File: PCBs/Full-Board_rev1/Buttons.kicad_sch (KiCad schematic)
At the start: 4 parts, among them SW1 SW_MEC_5E, SW2 SW_MEC_5E

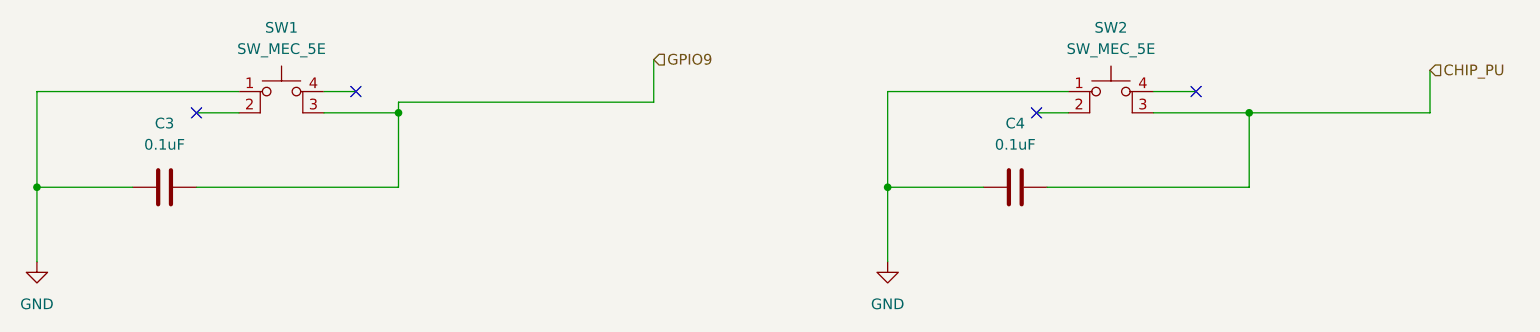
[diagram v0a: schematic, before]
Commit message: Added footprints for main board components
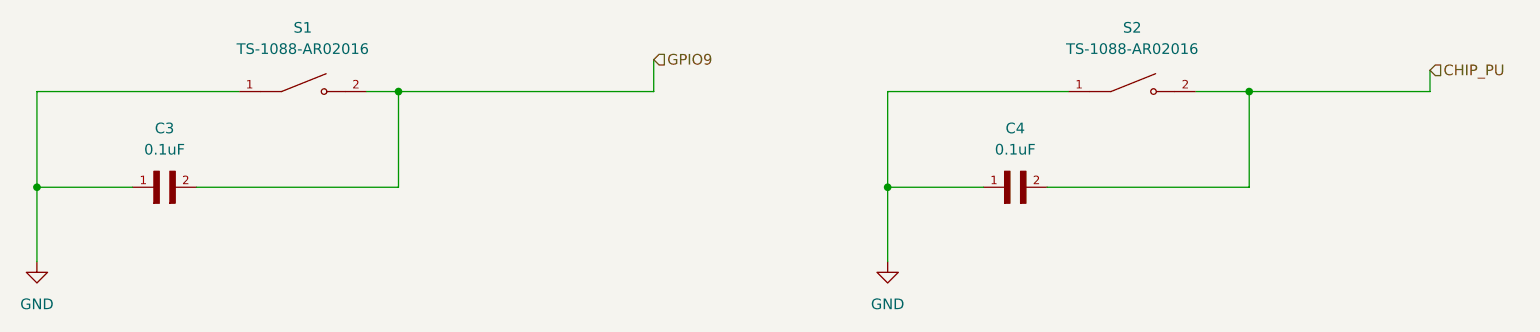
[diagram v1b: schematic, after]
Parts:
- removed C3, C4: 0.1uF, symbol Device:C
- removed SW1, SW2: SW_MEC_5E, symbol Switch:SW_MEC_5E
- added C3, C4: 0.1uF, FG26X7R1E106KRT06:CAPRB500W50L550T350H600, symbol FG26X7R1E106KRT06:FG26X7R1E106KRT06
- added S1, S2: TS-1088-AR02016, TS-1088-AR02016:SW_TS-1088-AR02016, symbol TS-1088-AR02016:TS-1088-AR02016
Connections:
- net CHIP_PU: now also C4.2, S2.2
- net GND: now also C3.1, C4.1, S1.1, S2.1
- net GPIO9: now also C3.2, S1.2
- no-connect marks 4 -> 0

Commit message: Changed capacitor footprints and added libs of same
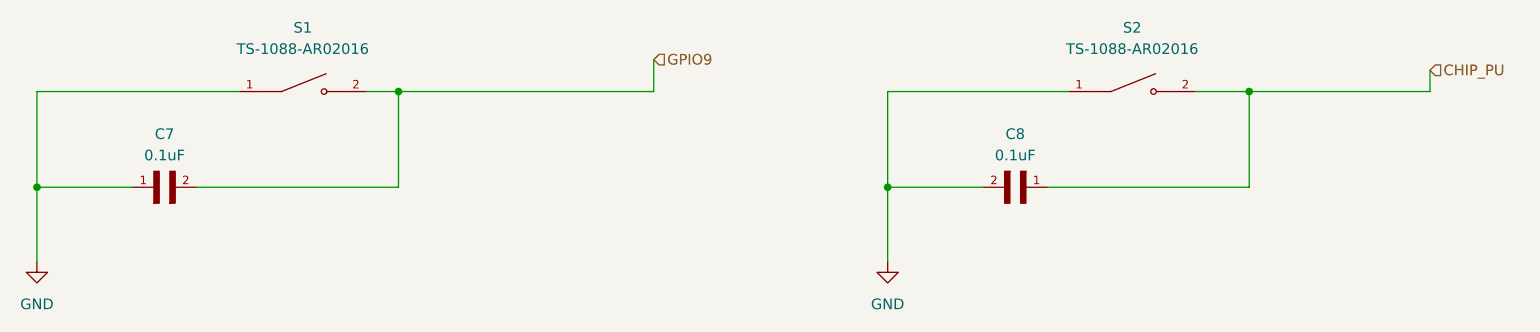
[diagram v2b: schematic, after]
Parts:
- removed C3, C4: 0.1uF, FG26X7R1E106KRT06:CAPRB500W50L550T350H600, symbol FG26X7R1E106KRT06:FG26X7R1E106KRT06
- added C7, C8: 0.1uF, FG28X7R1H104KNT06:CAPRB500W50L400T250H550, symbol FG28X7R1H104KNT06:FG28X7R1H104KNT06
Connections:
- net CHIP_PU: now also C8.1
- net GND: now also C7.1, C8.2
- net GPIO9: now also C7.2

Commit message: Redid some faulty footprint assignments
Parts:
- C7, C8: footprint FG28X7R1H104KNT06:CAPRB500W50L400T250H550 -> 100nCap:CAPRB500W50L400T250H550
- S1, S2: footprint TS-1088-AR02016:SW_TS-1088-AR02016 -> TactSwitch:SW_TS-1088-AR02016
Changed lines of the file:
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@@
 			)
 		)
-		(property "Footprint" "FG28X7R1H104KNT06:CAPRB500W50L400T250H550"
+		(property "Footprint" "100nCap:CAPRB500W50L400T250H550"
 			(at 69.85 102.87 0)
 			(effects
@@
 			)
 		)
-		(property "Footprint" "FG28X7R1H104KNT06:CAPRB500W50L400T250H550"
+		(property "Footprint" "100nCap:CAPRB500W50L400T250H550"
 			(at 173.99 102.87 0)
 			(effects
@@
 			)
 		)
-		(property "Footprint" "TS-1088-AR02016:SW_TS-1088-AR02016"
+		(property "Footprint" "TactSwitch:SW_TS-1088-AR02016"
 			(at 87.63 91.44 0)
 			(effects
@@
 			)
 		)
-		(property "Footprint" "TS-1088-AR02016:SW_TS-1088-AR02016"
+		(property "Footprint" "TactSwitch:SW_TS-1088-AR02016"
 			(at 186.69 91.44 0)
 			(effects
